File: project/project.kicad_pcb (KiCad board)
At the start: 4 copper layers, 84 x 84 mm, 162 parts, among them J101 BUS, J102 BUS, J103 Back, J104 Front, J105 FFC, J301 24V, J302 5V, J303 3V3, J304 6V, J401 USB_C_Receptacle_USB2.0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

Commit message: spritting up boards into separate repos
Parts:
- removed C102, C202, C203: 100n, Capacitor_SMD:C_0805_2012Metric_Pad1.18x1.45mm_HandSolder
- removed C201: 22u/25v, Capacitor_SMD:C_0805_2012Metric_Pad1.18x1.45mm_HandSolder
- removed C204, C205: 10u/50v, Capacitor_SMD:C_0805_2012Metric_Pad1.18x1.45mm_HandSolder
- removed D101: 6V8, Diode_SMD:D_SOD-323_HandSoldering
- removed D102, D103, D104, D105, D201, D202, D203, D204, D205, D206, D207, D208, D209, D210, D211, D212, D213, D214, D215, D216: RED, -local:LED_1206_3216Metric_ReverseMount
- removed H103, H104: thread, -local:post_m3x12.5mm
- removed J104: Front, Connector_PinHeader_2.54mm:PinHeader_2x08_P2.54mm_Vertical_SMD
- removed J105: FFC, -local:AFC11-S24ICC-00
- removed R101: 47k, Resistor_SMD:R_0805_2012Metric_Pad1.20x1.40mm_HandSolder
- removed R102: 10k, Resistor_SMD:R_0805_2012Metric_Pad1.20x1.40mm_HandSolder
- removed R103, R104, R105: 4k7, Resistor_SMD:R_0805_2012Metric_Pad1.20x1.40mm_HandSolder
- removed REF** (x4): toolhole, -local:toolhole
- removed SW101: SW_DIP_x04, -local:SW_DIP_SPSTx04_Slide_6.2x11.16mm_P2.54mm
- removed U102: GX101, Package_TO_SOT_SMD:SOT-23-6
- removed U201, U202: 74HC595, Package_SO:SOIC-16_3.9x9.9mm_P1.27mm
- removed U203, U204: ULN2803A, Package_SO:SOIC-18W_7.5x11.6mm_P1.27mm
- removed kibuzzard-67993413: G***, kibuzzard-67993413
- removed kibuzzard-67993427: G***, kibuzzard-67993427
- removed kibuzzard-67993436: G***, kibuzzard-67993436
- removed kibuzzard-67993449: G***, kibuzzard-67993449
- removed kibuzzard-67993459: G***, kibuzzard-67993459
- removed kibuzzard-679934A0: G***, kibuzzard-679934A0
- removed kibuzzard-679934B0: G***, kibuzzard-679934B0
- removed kibuzzard-679934DC: G***, kibuzzard-679934DC
- removed kibuzzard-679934EA: G***, kibuzzard-679934EA
- removed kibuzzard-67993507: G***, kibuzzard-67993507
- removed kibuzzard-67993514: G***, kibuzzard-67993514
- removed kibuzzard-67993518: G***, kibuzzard-67993518
- removed kibuzzard-6799352B: G***, kibuzzard-6799352B
- removed kibuzzard-67993537: G***, kibuzzard-67993537
- removed kibuzzard-67993543: G***, kibuzzard-67993543
- removed kibuzzard-67993570: G***, kibuzzard-67993570
- removed kibuzzard-6799357E: G***, kibuzzard-6799357E
- removed kibuzzard-67993590: G***, kibuzzard-67993590
- removed kibuzzard-6799359C: G***, kibuzzard-6799359C
- removed kibuzzard-679935A9: G***, kibuzzard-679935A9
- removed kibuzzard-679935B4: G***, kibuzzard-679935B4
- removed kibuzzard-679935C1: G***, kibuzzard-679935C1
- removed kibuzzard-6799365E: G***, kibuzzard-6799365E
- removed kibuzzard-67993A27: G***, kibuzzard-67993A27
- removed kibuzzard-68F6C81E: G***, kibuzzard-68F6C81E
- removed kibuzzard-68F6C83B: G***, kibuzzard-68F6C83B
- removed kibuzzard-68F6C9D1: G***, kibuzzard-68F6C9D1
- removed kibuzzard-68F6C9D9: G***, kibuzzard-68F6C9D9
- added kibuzzard-69BC0404: G***, kibuzzard-69BC0404, F.Cu at (185.3, 81.0)
- added kibuzzard-69BC0AB2: G***, kibuzzard-69BC0AB2, B.Cu at (182.0, 118.5)
- added kibuzzard-69BC0AB9: G***, kibuzzard-69BC0AB9, B.Cu at (114.0, 118.5)
- added kibuzzard-69BC0BA6: G***, kibuzzard-69BC0BA6, B.Cu at (148.5, 88.3)
- moved C310 39.9 mm to (171.8, 107.3)
- moved C405 39.9 mm to (117.8, 83.5)
- moved C406 39.9 mm to (119.8, 83.5)
- moved C408 39.9 mm to (121.7, 94.3)
- moved J102 39.9 mm to (185.4, 104.8)
- moved J301 39.9 mm to (175.2, 98.4)
- moved J303 39.9 mm to (125.0, 110.0)
- moved R306 39.9 mm to (160.6, 112.3)
- moved R411 39.9 mm to (160.2, 105.3)
- moved C301 39.9 mm to (164.0, 106.9)
- moved C304 39.9 mm to (176.6, 111.5)
- moved C305 39.9 mm to (176.6, 109.5)
- moved C306 39.9 mm to (176.6, 107.5)
- moved C308 39.9 mm to (130.0, 111.0)
- moved C309 39.9 mm to (127.0, 114.0)
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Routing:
- net F_24V: track 143.1 -> 0.00 mm, vias 8 -> 0
- net F_5V: track 84.6 -> 0.00 mm, vias 4 -> 0
- net Net-(D216-Pad1): track 82.9 -> 0.00 mm, vias 4 -> 0
- net /driver/R3: track 82.8 -> 0.00 mm, vias 4 -> 0
- net /driver/R9: track 79.6 -> 0.00 mm, vias 4 -> 0
- net Net-(D207-Pad1): track 78.3 -> 0.00 mm, vias 2 -> 0
- net Net-(D208-Pad1): track 78.0 -> 0.00 mm, vias 4 -> 0
- net Net-(D201-Pad1): track 75.7 -> 0.00 mm, vias 6 -> 0
- net /driver/R2: track 74.0 -> 0.00 mm, vias 2 -> 0
- net Net-(D215-Pad1): track 73.6 -> 0.00 mm, vias 2 -> 0
- net /driver/R10: track 71.2 -> 0.00 mm, vias 2 -> 0
- net Net-(D214-Pad1): track 68.6 -> 0.00 mm, vias 4 -> 0
- net Net-(D212-Pad1): track 66.6 -> 0.00 mm
- net /driver/R1: track 65.8 -> 0.00 mm, vias 2 -> 0
- net /driver/O_DATA: track 63.9 -> 0.00 mm
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- removed copper zone on B.Cu, net F_GND
- removed copper zone on F.Cu, net F_GND
- removed copper zone on In1.Cu, net F_GND
- removed copper zone on In2.Cu, net F_GND
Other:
- board size 84 x 84 mm -> 84 x 41 mm
- board text removed: "3V3 GND GND DATA GND CLOCK 5V 24V"
- board text removed: "3V3 GND GND GND GND R14 R12 R10 R8 R6 R4 R2"
- board text removed: "IN"
- board text removed: "JLCJLCJLCJLC"
- board text removed: "OUT"
- board text removed: "SDA SCL 24V 24V R15 R13 R11 R9 R7 R5 R3 R1"

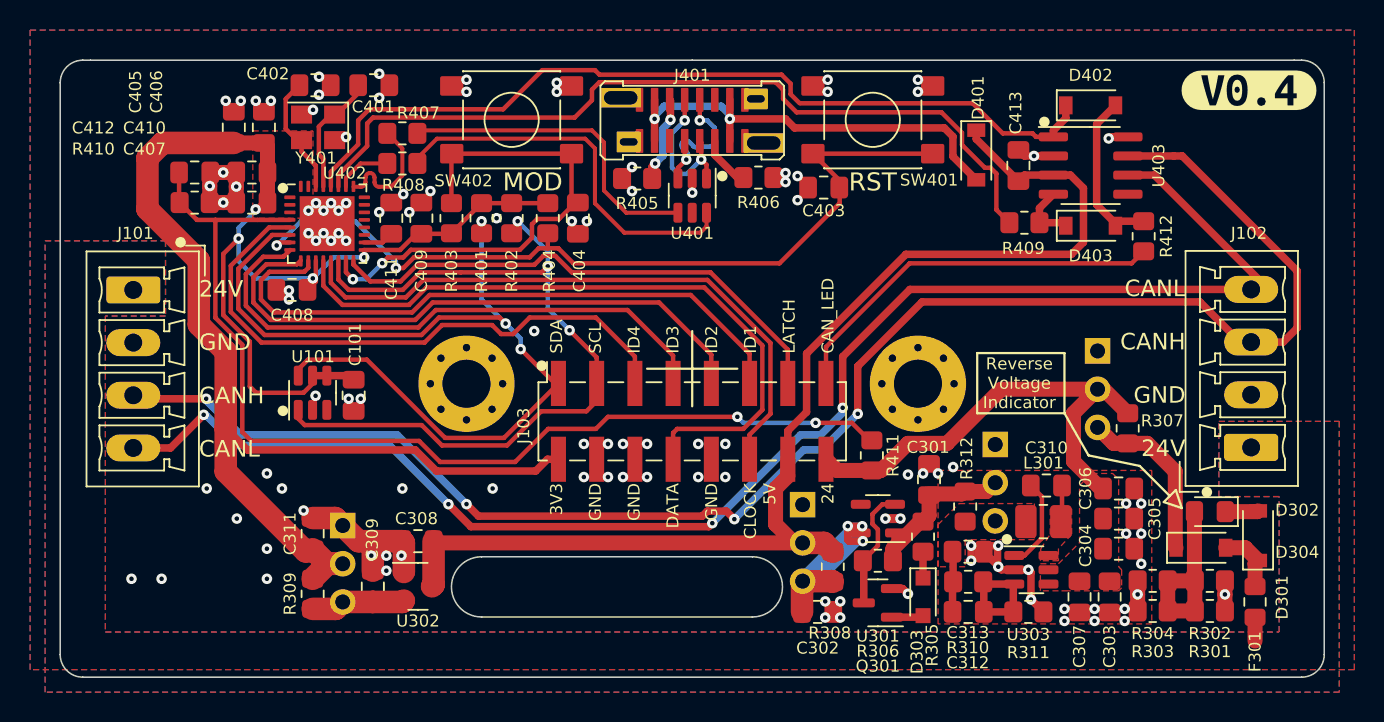
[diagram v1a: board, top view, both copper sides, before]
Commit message: part consolidation and QoL improvements
* Using same crystal as in other projects
* Switching to TMP102 as TMP101 is no longer available
* Adding cutouts to make assembly esier
* Making net names more readable
* bumping up version
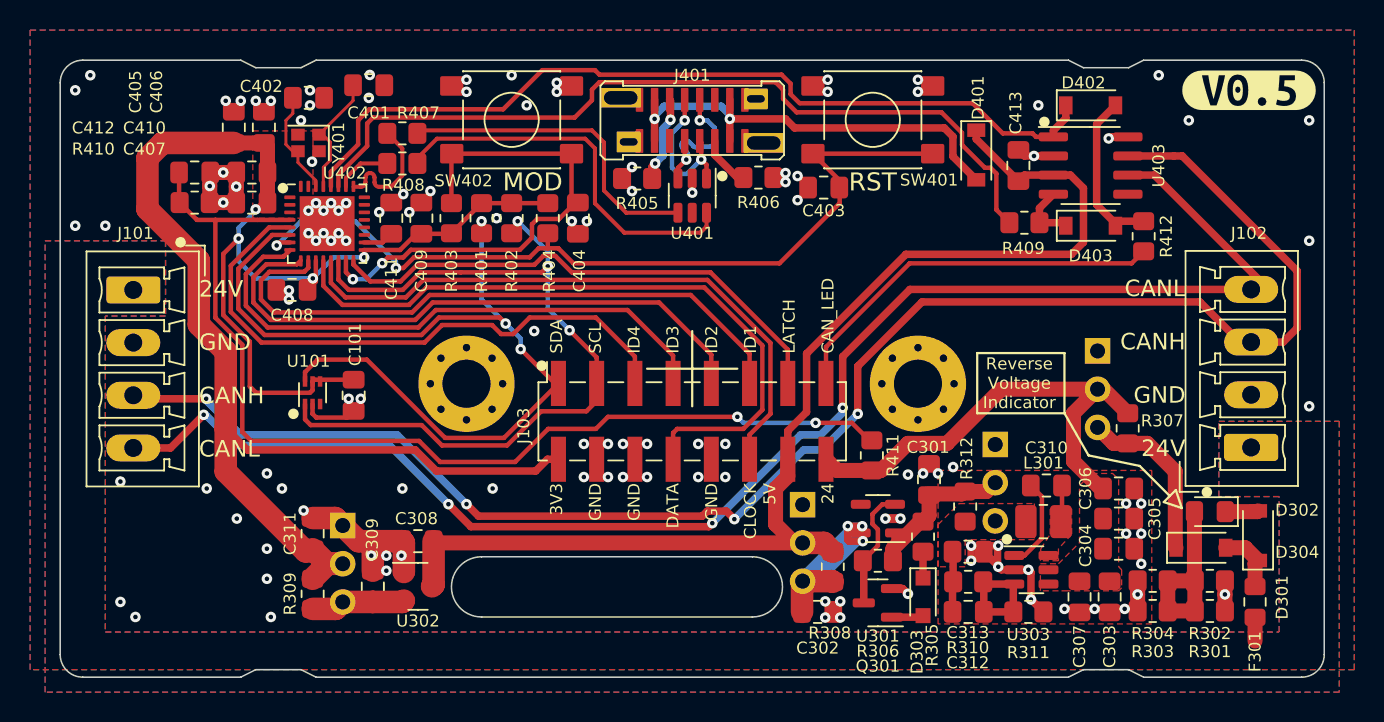
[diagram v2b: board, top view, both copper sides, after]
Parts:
- removed kibuzzard-69BC0404: G***, kibuzzard-69BC0404
- removed kibuzzard-69BC0AB2: G***, kibuzzard-69BC0AB2
- added kibuzzard-69BC2E2E: G***, kibuzzard-69BC2E2E, F.Cu at (185.3, 81.0)
- added kibuzzard-69BC2E41: G***, kibuzzard-69BC2E41, B.Cu at (182.0, 118.5)
- U101: value GX101 -> TMP102; footprint Package_TO_SOT_SMD:SOT-23-6 -> -local:SOT-563
- Y401: footprint Crystal:Crystal_SMD_3225-4Pin_3.2x2.5mm -> -local:Crystal_SMD_2016-4Pin_2.0x1.6mm
- moved Y401 1.22 mm to (122.8, 84.5)
- moved C402 0.94 mm to (122.8, 81.5)
- moved C401 0.34 mm to (126.8, 80.7)
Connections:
- net B_24V renamed 24V
- net B_3V3 renamed 3V3
- net B_5V renamed 5V
- net B_CAN_LED renamed CAN_LED
- net B_CLOCK renamed CLOCK
- net B_DATA renamed DATA
- net B_GND renamed GND
- net B_ID1 renamed ID1
- net B_ID2 renamed ID2
- net B_ID3 renamed ID3
- net B_ID4 renamed ID4
- net B_LATCH renamed LATCH
- net B_SCL renamed SCL
- net B_SDA renamed SDA
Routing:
- net GND: track 38.5 -> 42.1 mm, vias 113 -> 123
- net /uC/XTAL_P: track 8.01 -> 7.11 mm
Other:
- outline, holes or cut-outs redrawn

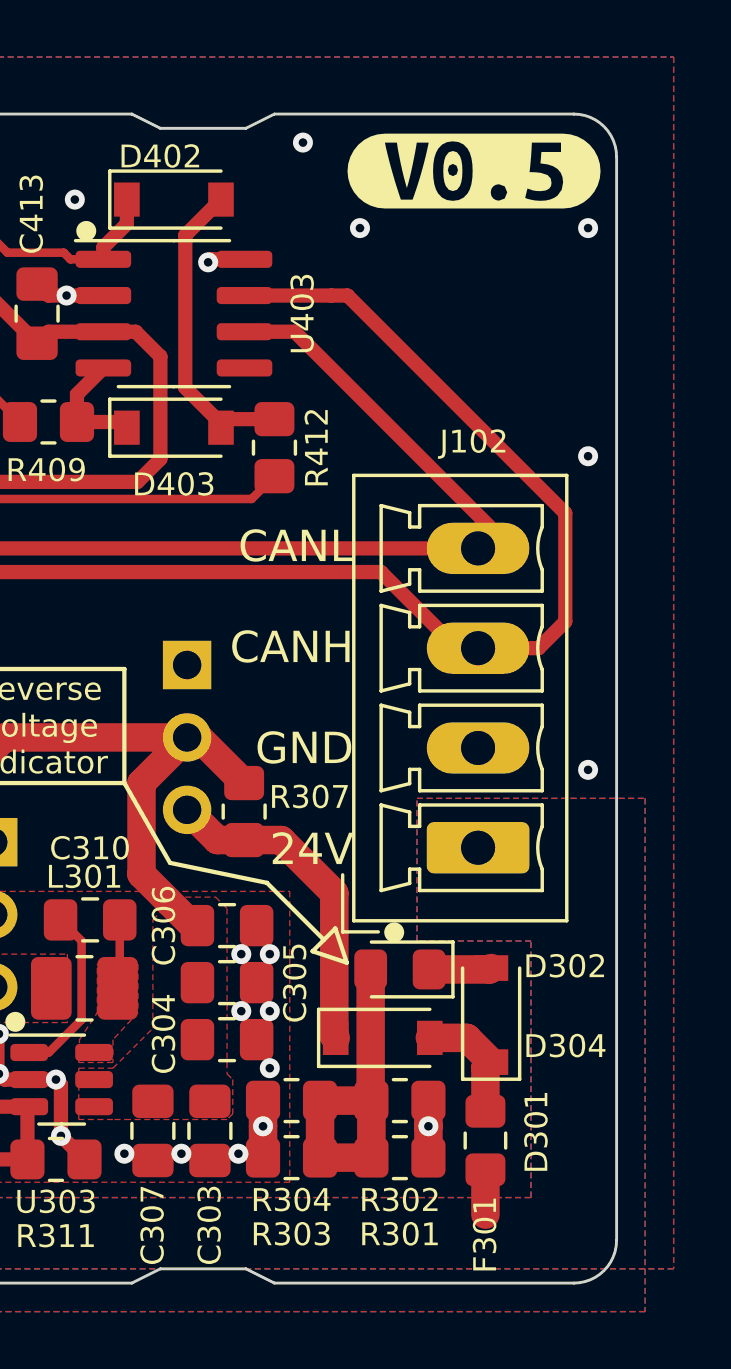
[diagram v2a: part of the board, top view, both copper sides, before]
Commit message: adding cutout for easier assembly
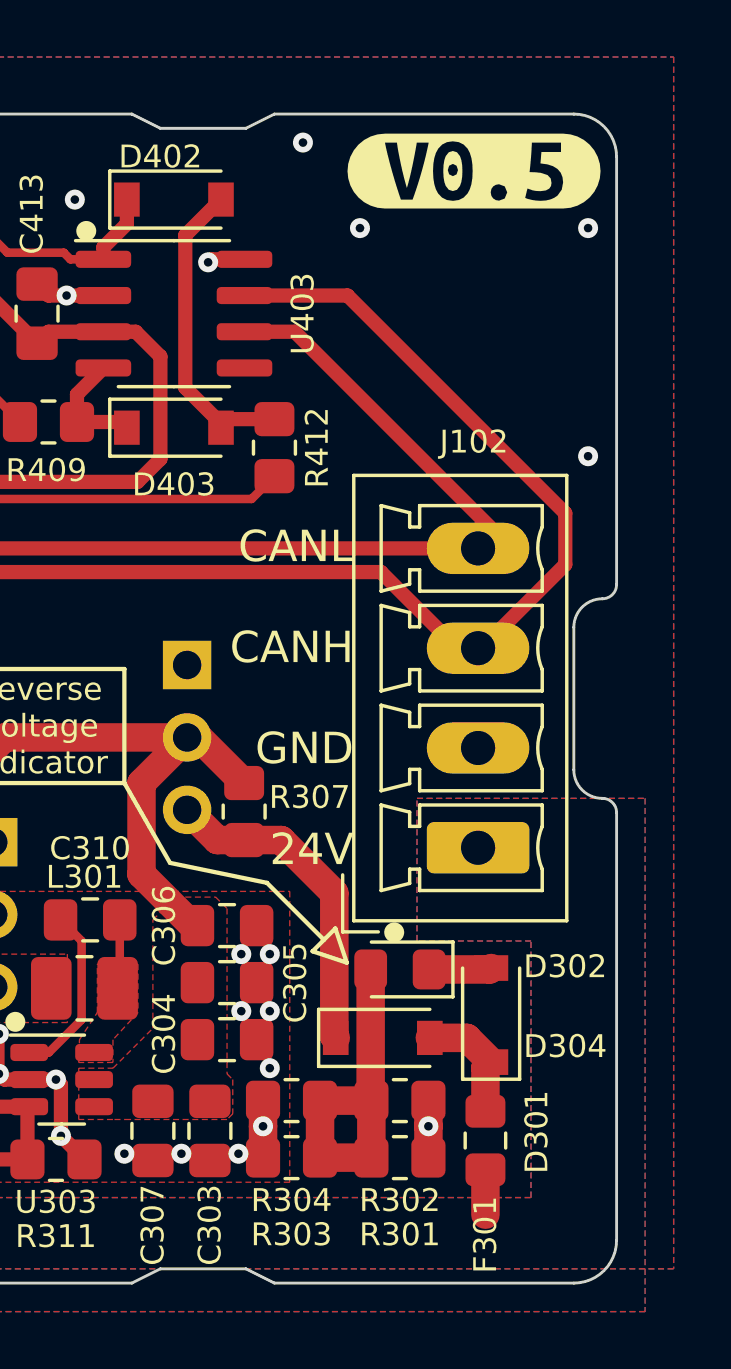
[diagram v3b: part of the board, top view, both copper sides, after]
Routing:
- net /uC/CANH: track 108.6 -> 107.5 mm
- net GND: vias 123 -> 122
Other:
- outline, holes or cut-outs redrawn

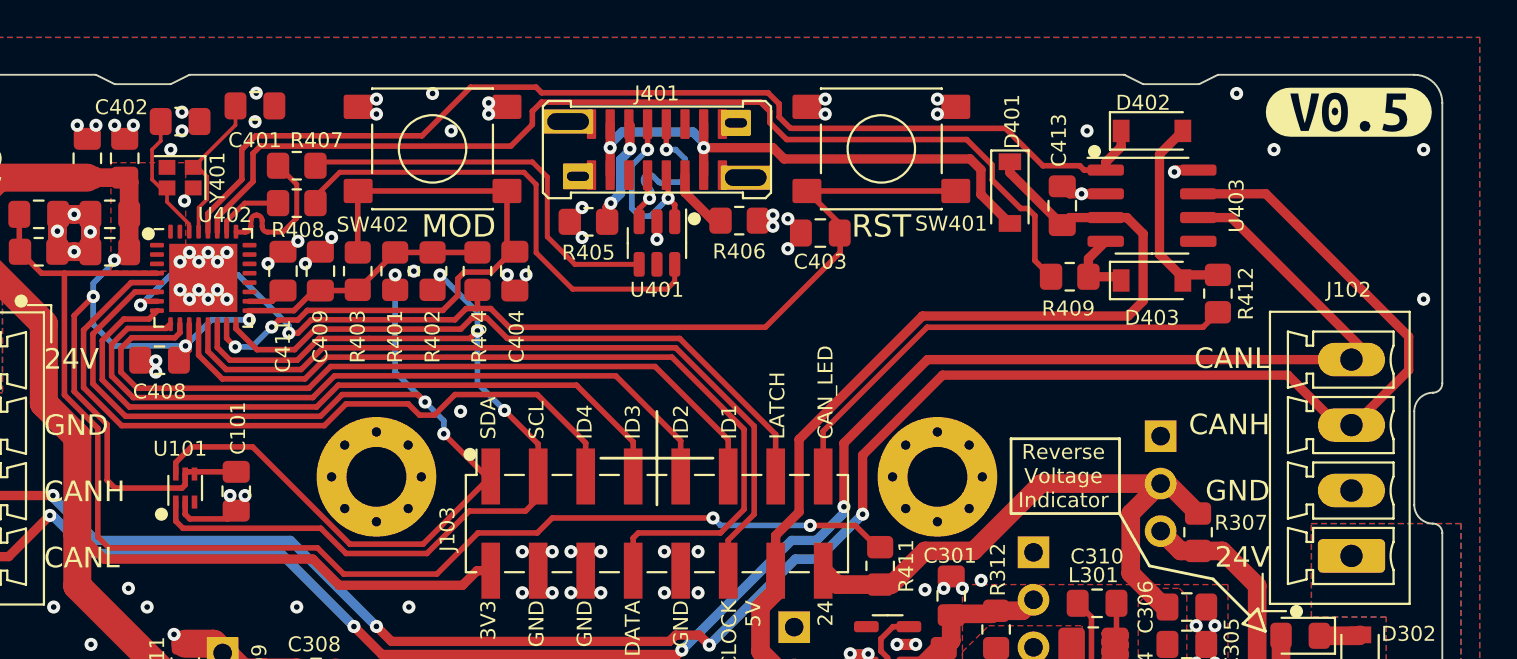
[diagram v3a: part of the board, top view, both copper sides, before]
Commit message: fixing tmp102 pinout
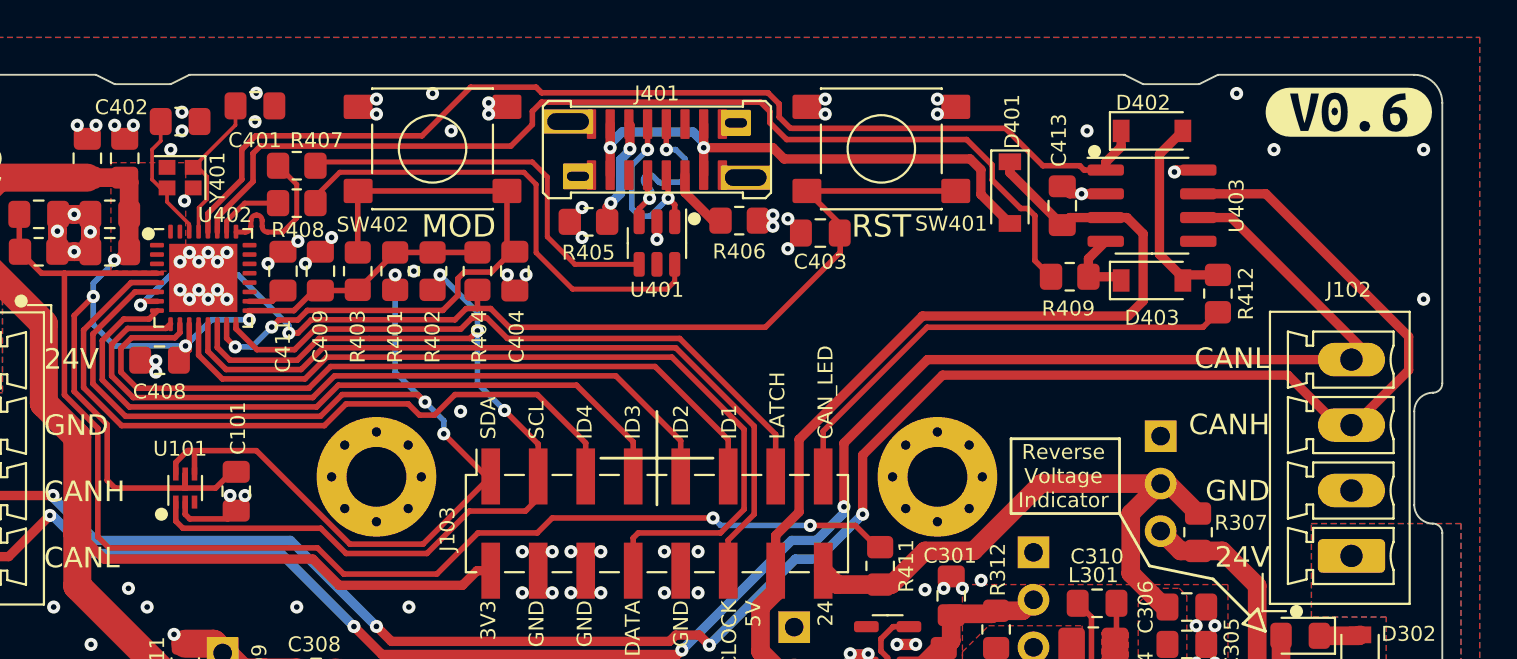
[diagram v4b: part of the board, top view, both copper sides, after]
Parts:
- removed kibuzzard-69BC2E2E: G***, kibuzzard-69BC2E2E
- removed kibuzzard-69BC2E41: G***, kibuzzard-69BC2E41
- added kibuzzard-69E609FA: G***, kibuzzard-69E609FA, F.Cu at (185.3, 81.0)
- added kibuzzard-69E60A07: G***, kibuzzard-69E60A07, B.Cu at (182.0, 118.5)
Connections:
- U101 pad 4: 3V3 -> SDA
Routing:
- net SDA: track 61.5 -> 62.9 mm
- net 3V3: track 121.7 -> 122.7 mm
